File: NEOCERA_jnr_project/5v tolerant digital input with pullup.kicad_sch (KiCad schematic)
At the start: 3 parts, among them U3 74AHCT1G126

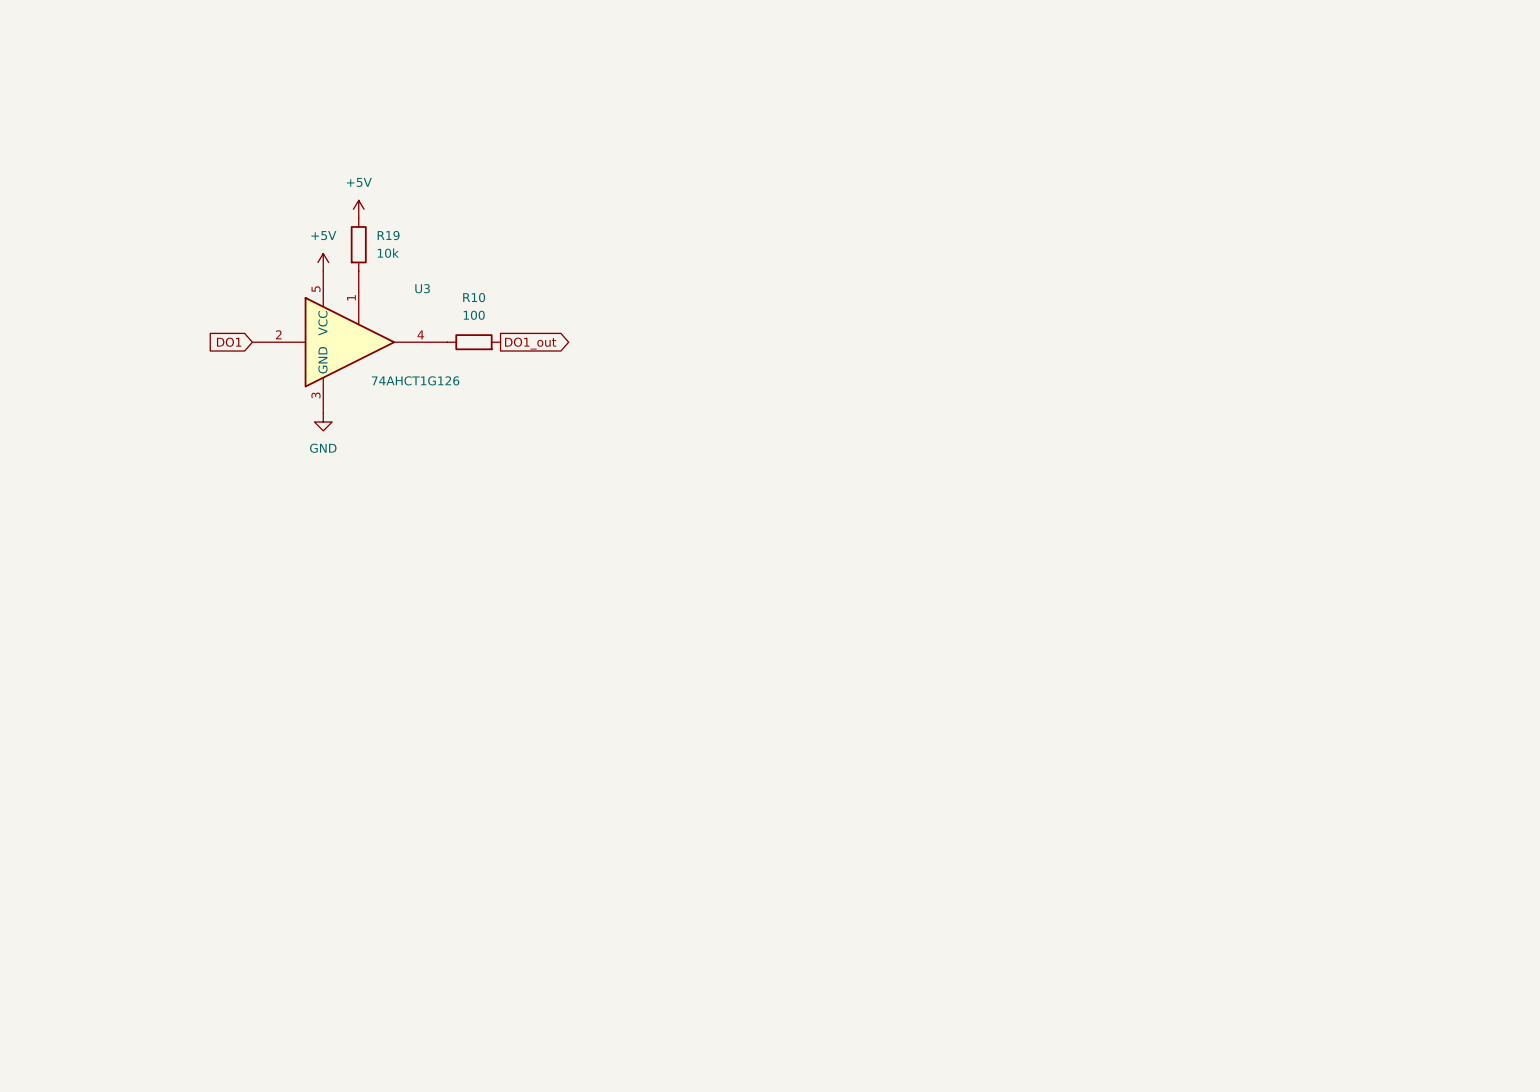
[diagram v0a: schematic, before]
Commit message: updated al the amounts of each item in the schematic
made updates in the amount of each components
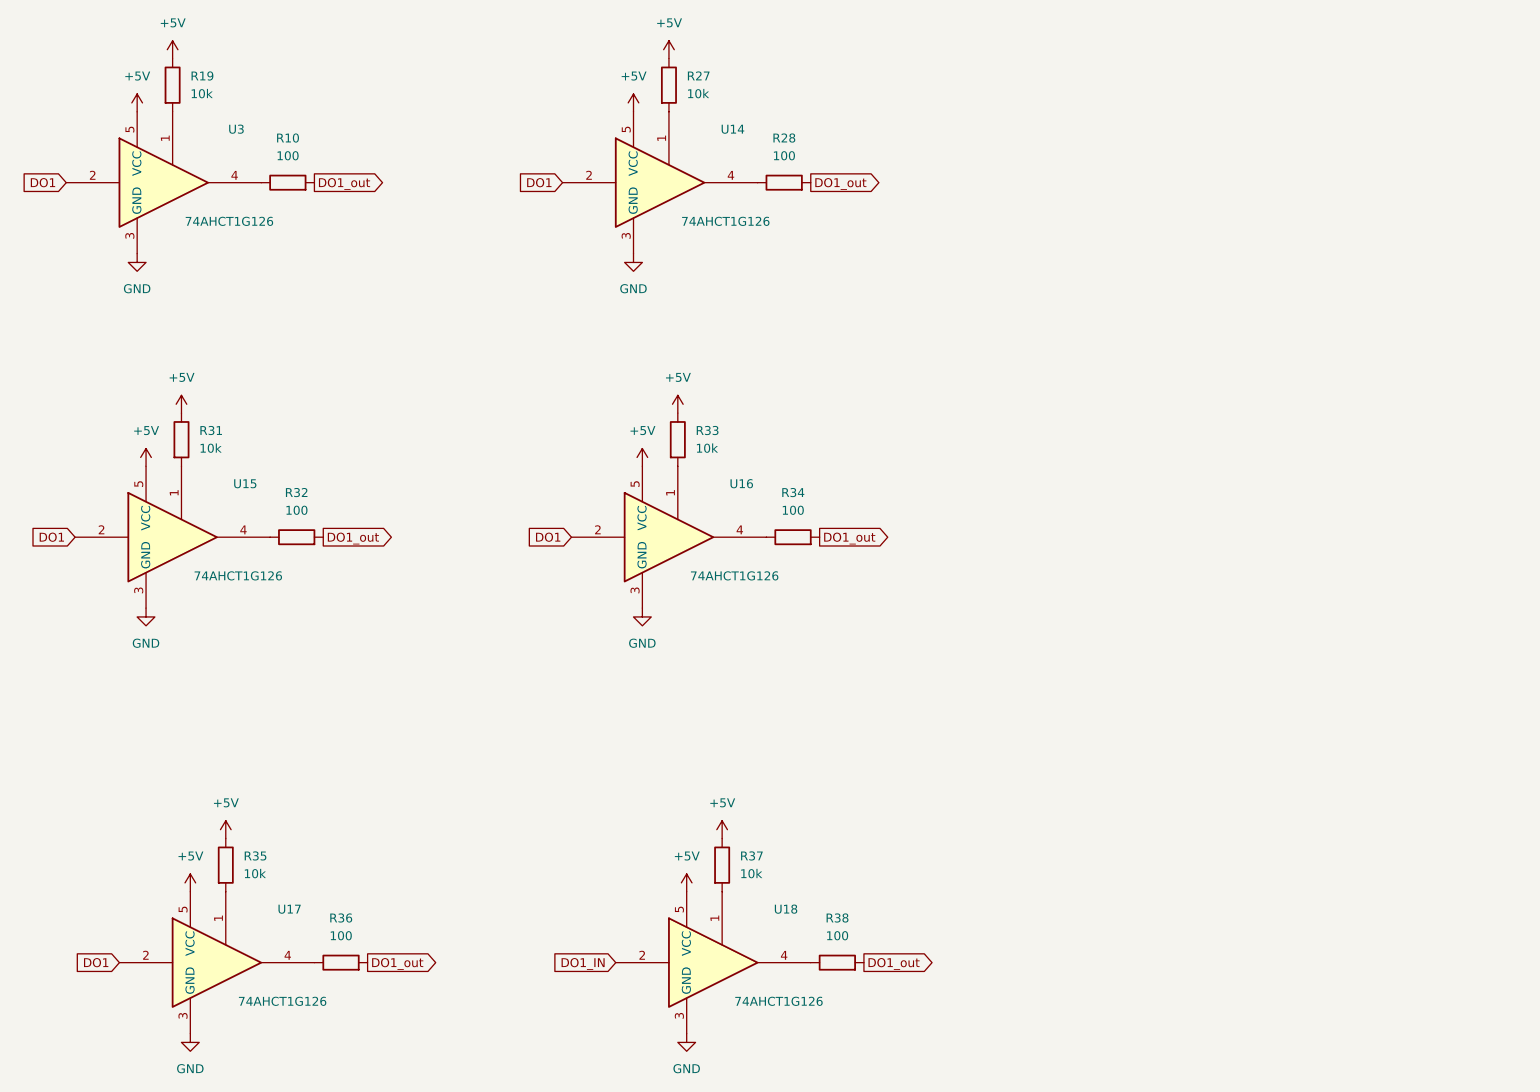
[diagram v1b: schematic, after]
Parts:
- added R27, R31, R33, R35, R37: 10k, Resistor_SMD:R_0603_1608Metric_Pad0.98x0.95mm_HandSolder, symbol Device:R
- added R28, R32, R34, R36, R38: 100, Resistor_SMD:R_0603_1608Metric_Pad0.98x0.95mm_HandSolder, symbol Device:R
- added U14, U15, U16, U17, U18: 74AHCT1G126, Package_TO_SOT_SMD:SOT-23-5_HandSoldering, symbol 74xGxx:74AHCT1G126
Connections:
- net +5V: now also R27.1, R31.1, R33.1, R35.1, R37.1, U14.5 (VCC), U15.5 (VCC), U16.5 (VCC), U17.5 (VCC), U18.5 (VCC)
- net DO1: now also U14.2, U15.2, U16.2, U17.2
- net DO1_out: now also R28.2, R32.2, R34.2, R36.2, R38.2
- net GND: now also U14.3 (GND), U15.3 (GND), U16.3 (GND), U17.3 (GND), U18.3 (GND)
- new net: R35.2, U17.1
- new net: R38.1, U18.4
- new net: R31.2, U15.1
- new net: R32.1, U15.4
- new net: R27.2, U14.1
- new net: R37.2, U18.1
- new net: R33.2, U16.1
- new net: R28.1, U14.4
- new net: R36.1, U17.4
- new net: R34.1, U16.4
- new net DO1_IN: U18.2
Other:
- moved on the sheet: R10, R19, U3

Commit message: Edits made with Dr. Caw.
I added the net to the root
I added the write global nets to some of the previously designed symbols like TX/RX
I added a 3.3V pullup resistor to the opto
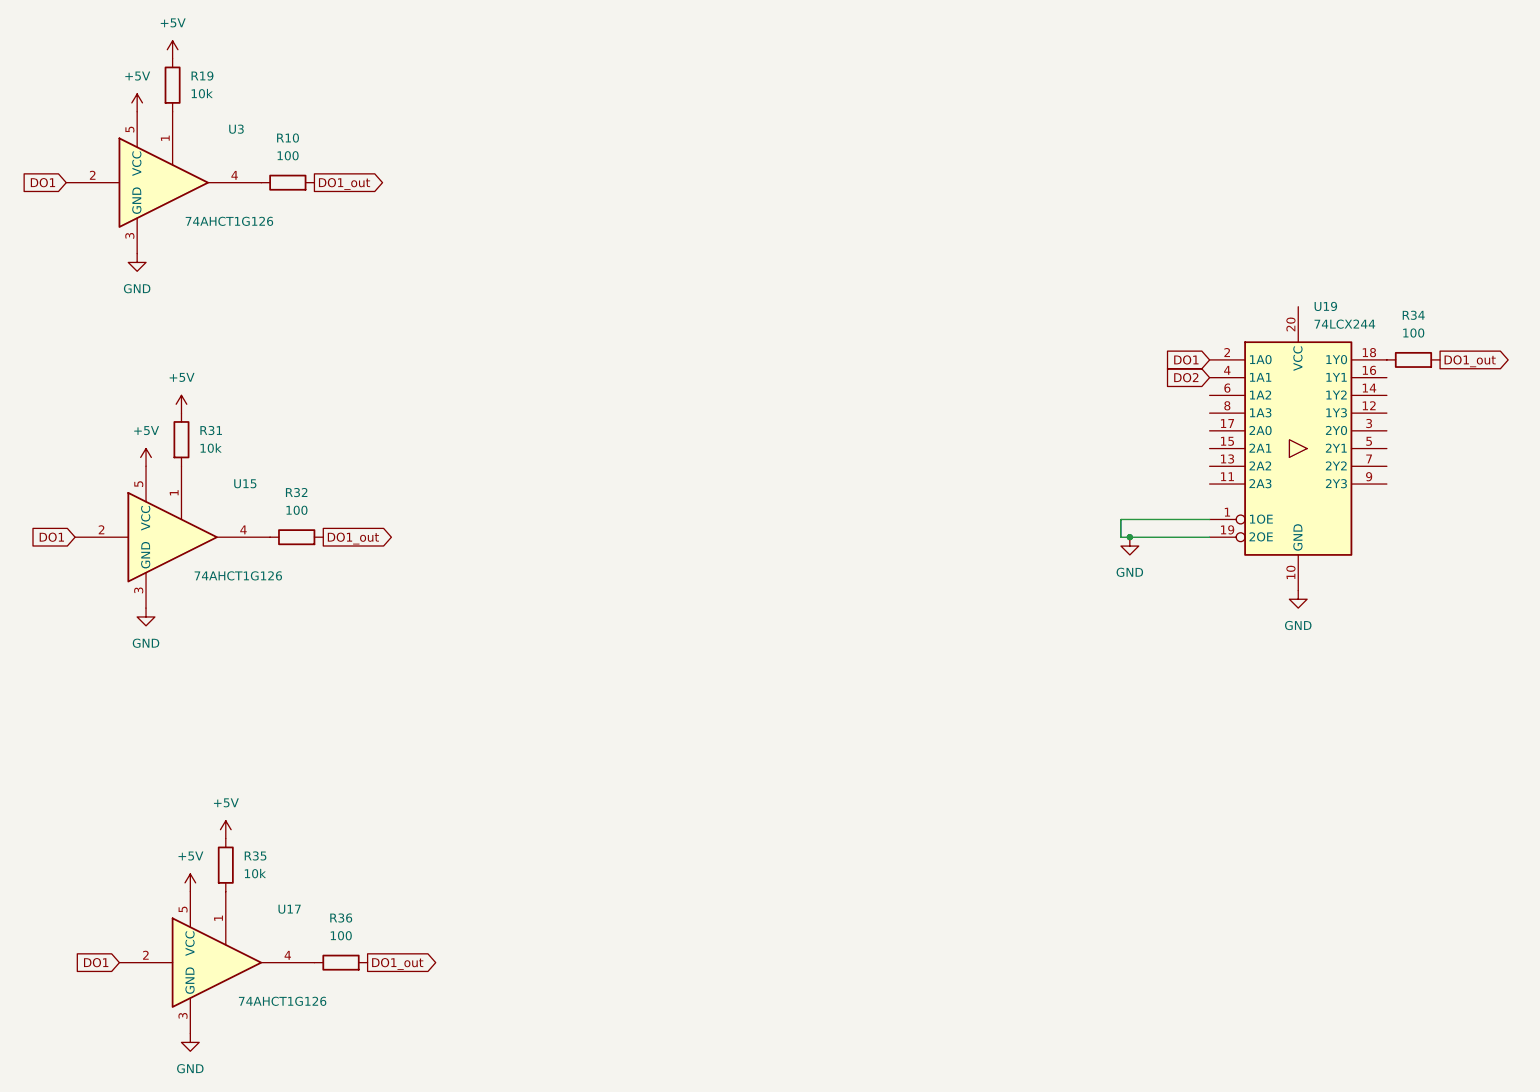
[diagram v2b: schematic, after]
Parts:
- removed R27, R33, R37: 10k, Resistor_SMD:R_0603_1608Metric_Pad0.98x0.95mm_HandSolder, symbol Device:R
- removed R28, R38: 100, Resistor_SMD:R_0603_1608Metric_Pad0.98x0.95mm_HandSolder, symbol Device:R
- removed U14, U16, U18: 74AHCT1G126, Package_TO_SOT_SMD:SOT-23-5_HandSoldering, symbol 74xGxx:74AHCT1G126
- added U19: 74LCX244, symbol 74xx:74HCT244
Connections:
- net DO1: now also U19.2 (1A0)
- net GND: now also U19.1 (1OE), U19.10 (GND), U19.19 (2OE)
- net at R34.1: now also U19.18 (1Y0)
- new net DO2: U19.4 (1A1)
